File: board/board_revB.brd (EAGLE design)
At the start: 94 x 44.5 mm, 88 parts, among them IC1 MCP1703CB, Q1 ULN2003AS, Q2 ULN2003AD, Y1 8Mhz

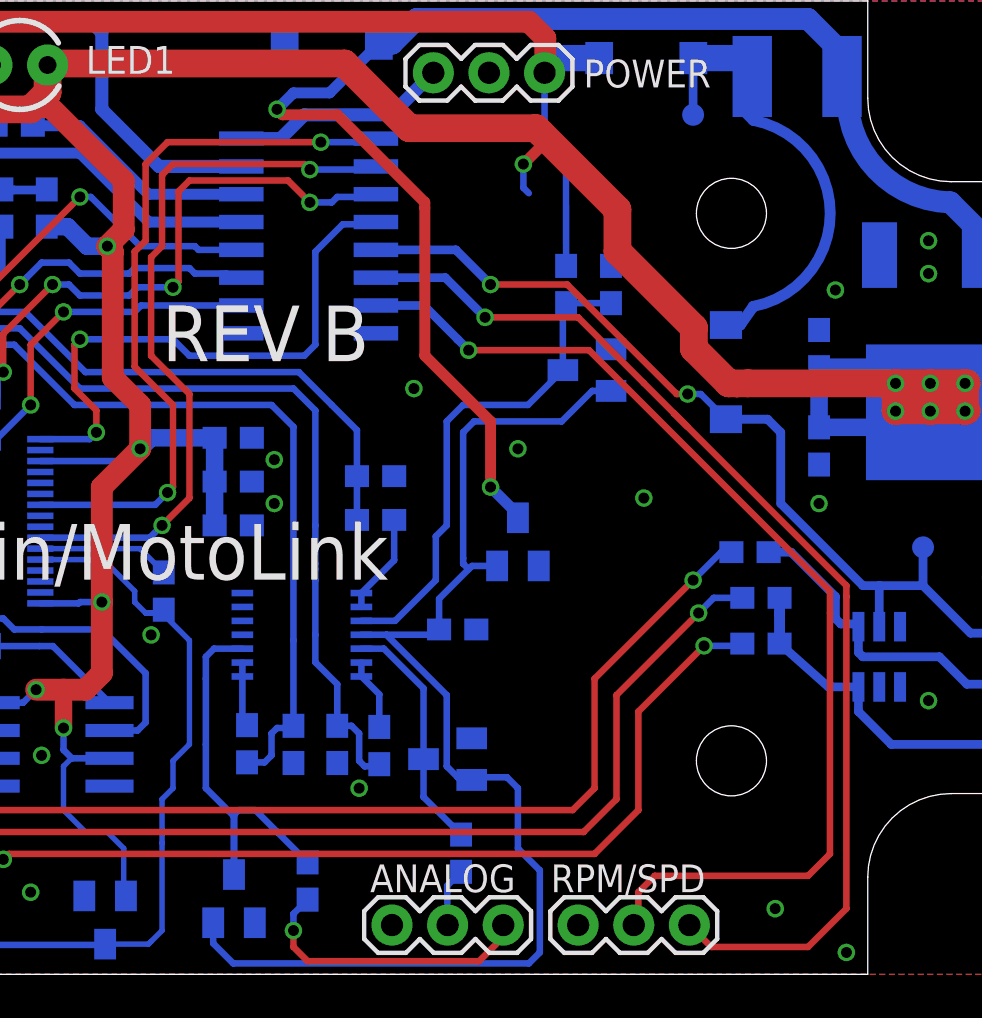
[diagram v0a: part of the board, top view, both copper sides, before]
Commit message: [Code] Now using CCM for ISRs and time critical threads
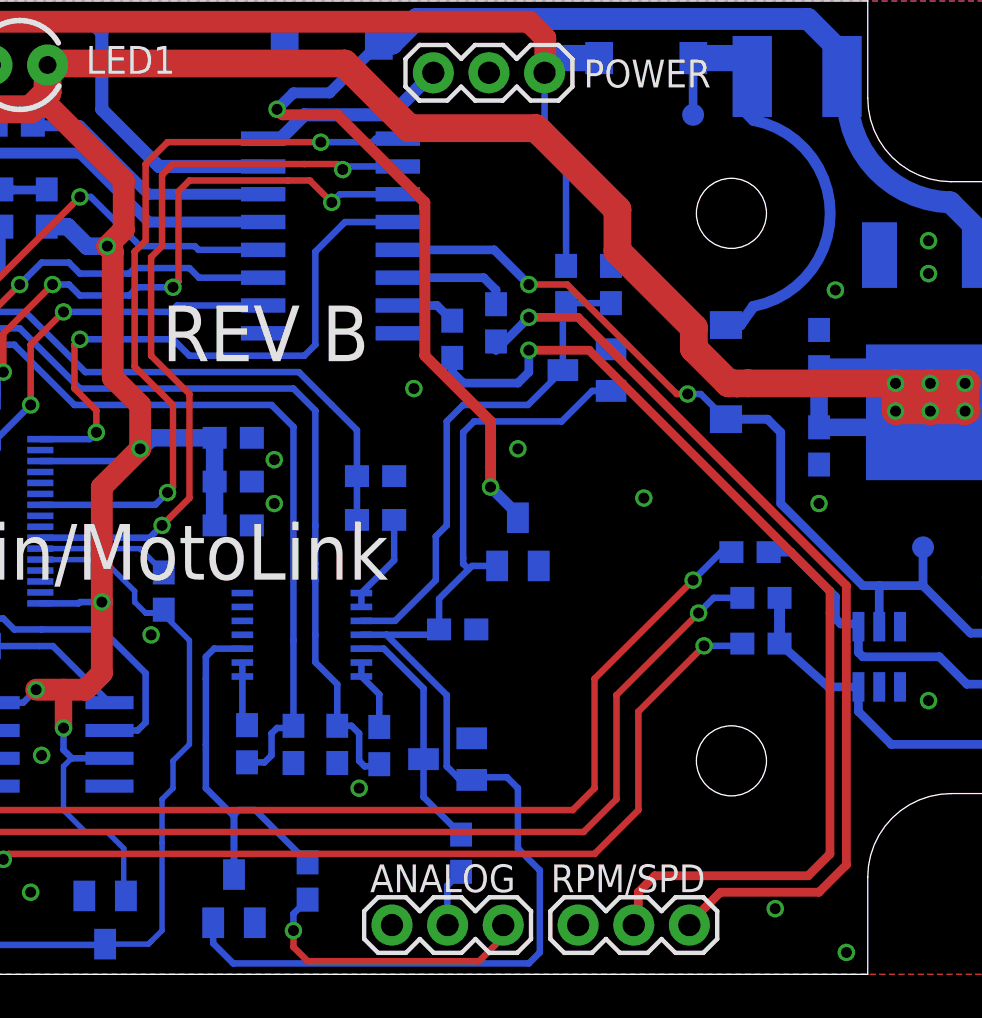
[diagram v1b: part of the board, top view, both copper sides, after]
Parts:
- added R25, R26: 1K, SparkFun-Resistors:0603-RES
- moved Q2 1.00 mm to (61.2, 33.7)
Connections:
- new net N$12: CON_RPM-VSS.3, R25.1
- new net N$9: Q2.7, R26.2
- net N$16: now also R25.2; no longer CON_RPM-VSS.3
- net N$21: now also R26.1; no longer Q2.7
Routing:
- net N$16: track 51.3 -> 5.37 mm, vias 1 -> 0
- net N$12: track 0.00 -> 43.2 mm, vias 0 -> 1
- net N$9: track 0.00 -> 2.77 mm
- net +3V3: track 305.6 -> 303.1 mm, vias 16 -> 15
- net N$21: track 49.2 -> 46.9 mm
- net FREQ1_IN: track 29.0 -> 30.0 mm
- net SCS_TRIG: track 33.3 -> 34.4 mm
- net LED1_TRIG: track 26.2 -> 27.3 mm
- net LED2_TRIG: track 26.3 -> 27.3 mm
- net USB_VBUS: track 41.6 -> 40.6 mm
- net USB_DETECT: track 24.1 -> 25.1 mm
- net SCS: track 69.7 -> 70.7 mm
- net RELAY_TRIG: track 33.1 -> 34.1 mm
- net RELAY_OUT: track 10.0 -> 9.01 mm
- net N$15: track 10.8 -> 11.8 mm
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
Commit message: [Board] Updates
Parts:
- added ESP: ESP8266, misc:ESP-03
- IC_FRAM: value 25LC080SN -> FM25L04B
- renumbered IC_EE to IC_FRAM
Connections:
- net GND: now also IC_OPA.12, IC_OPA.13
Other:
- board text added: "Github.com /fpoussin /MotoLink"
- board text removed: "Github.com/fpoussin/MotoLink"
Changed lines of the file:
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@@
 <wire x1="89.535" y1="36.195" x2="93.98" y2="36.195" width="0" layer="20"/>
 <wire x1="93.98" y1="36.195" x2="93.98" y2="8.255" width="0" layer="20"/>
-<text x="16.3125" y="21.33" size="3.81" layer="21" font="vector" ratio="16">MotoLink</text>
-<text x="16.2075" y="18.025" size="2.54" layer="21" font="vector" ratio="16" distance="0">Github.com/fpoussin/MotoLink</text>
+<text x="18.8125" y="21.33" size="3.81" layer="21" font="vector" ratio="16">MotoLink</text>
+<text x="73.2075" y="19.525" size="2.54" layer="21" font="vector" ratio="14" distance="30">Github.com
+/fpoussin
+/MotoLink</text>
 <wire x1="30.955" y1="14.94" x2="40.6625" y2="14.94" width="0.254" layer="21"/>
 <wire x1="40.6625" y1="14.94" x2="40.6625" y2="4.4625" width="0.254" layer="21"/>
@@
 <text x="23.3825" y="8.495" size="1.27" layer="21" font="vector" ratio="16" rot="R180">1</text>
 <text x="29.99" y="4.245" size="1.27" layer="21" font="vector" ratio="16" rot="R180">6</text>
-<text x="53.5" y="28" size="2.54" layer="21" font="vector" ratio="14" distance="40">REV B</text>
+<text x="25" y="18" size="2.54" layer="21" font="vector" ratio="14" distance="30">REV B</text>
 <text x="5.25" y="24.25" size="1.27" layer="25" font="vector" ratio="16" rot="R90">K-LINE</text>
 <text x="5.25" y="18" size="1.27" layer="25" font="vector" ratio="16" rot="R90">CAN</text>
@@
 <attribute name="VALUE" x="84.75" y="38.025" size="1.016" layer="28" rot="MR0"/>
 </element>
-<element name="IC_EE" library="microchip" package="SO-08" value="25LC080SN" x="48.5" y="10.5" smashed="yes" rot="MR270">
+<element name="IC_FRAM" library="microchip" package="SO-08" value="FM25L04B" x="48.5" y="10.5" smashed="yes" rot="MR270">
 <attribute name="OC_NEWARK" value="96K4092" x="48.5" y="10.5" size="1.778" layer="28" rot="MR270" display="off"/>
 <attribute name="MPN" value="25LC080/SN" x="48.5" y="10.5" size="1.778" layer="28" rot="MR270" display="off"/>
 <attribute name="MF" value="MICROCHIP" x="48.5" y="10.5" size="1.778" layer="28" rot="MR270" display="off"/>
 <attribute name="OC_FARNELL" value="1137302" x="48.5" y="10.5" size="1.778" layer="28" rot="MR270" display="off"/>
-<attribute name="NAME" x="51.405" y="13.417" size="1.27" layer="26" font="vector" ratio="16" rot="MR0"/>
+<attribute name="NAME" x="52.655" y="13.417" size="1.27" layer="26" font="vector" ratio="16" rot="MR0"/>
 <attribute name="VALUE" x="50.405" y="6.563" size="1.27" layer="28" rot="MR0"/>
 </element>
@@
 <attribute name="VALUE" x="65.607" y="27.984" size="0.4064" layer="28" font="vector" rot="MR90"/>
 </element>
+<element name="ESP" library="misc" package="ESP-03" value="ESP8266" x="64.5" y="17.75"/>
 </elements>
 <signals>
@@
 <contactref element="C6" pad="2"/>
 <contactref element="C8" pad="1"/>
-<via x="53" y="15.5" extent="1-16" drill="0.5"/>
+<via x="53" y="15.25" extent="1-16" drill="0.5"/>
 <via x="39.75" y="20.75" extent="1-16" drill="0.5"/>
 <via x="11.5" y="39.5" extent="1-16" drill="0.5"/>
@@
 <via x="38.25" y="9.25" extent="1-16" drill="0.5"/>
 <via x="48" y="10" extent="1-16" drill="0.5"/>
-<via x="62.5" y="8.5" extent="1-16" drill="0.5"/>
-<via x="81.5" y="3" extent="1-16" drill="0.5"/>
+<via x="60.5" y="12.75" extent="1-16" drill="0.5"/>
 <via x="88.5" y="32" extent="1-16" drill="0.5"/>
 <via x="32" y="34.25" extent="1-16" drill="0.5"/>
@@
 <via x="1" y="16.5" extent="1-16" drill="0.5"/>
 <via x="4.25" y="33.25" extent="1-16" drill="0.5"/>
-<contactref element="IC_EE" pad="4"/>
+<contactref element="IC_FRAM" pad="4"/>
 <contactref element="R20" pad="2"/>
 <contactref element="R19" pad="2"/>
@@
 <contactref element="IC1" pad="1"/>
 <via x="84.75" y="1" extent="1-16" drill="0.5"/>
+<via x="68.25" y="36" extent="1-16" drill="0.5"/>
+<contactref element="IC_OPA" pad="12"/>
+<contactref element="IC_OPA" pad="13"/>
 </signal>
 <signal name="+3V3">
@@
 <wire x1="41.725" y1="41.525" x2="41.7" y2="41.5" width="1.27" layer="1"/>
 <wire x1="70.8025" y1="38.4175" x2="70.8025" y2="37.8025" width="0.3" layer="1"/>
-<wire x1="47.94" y1="16.94" x2="49.69" y2="16.94" width="0.3" layer="16"/>
-<wire x1="49.69" y1="16.94" x2="49.75" y2="17" width="0.3" layer="16"/>
-<wire x1="49.75" y1="17" x2="50.75" y2="17" width="0.3" layer="16"/>
+<wire x1="47.94" y1="16.94" x2="50.69" y2="16.94" width="0.3" layer="16"/>
+<wire x1="50.69" y1="16.94" x2="50.75" y2="17" width="0.3" layer="16"/>
 <via x="50.75" y="17" extent="1-16" drill="0.5"/>
 <wire x1="50.75" y1="17" x2="50.75" y2="22.25" width="1" layer="1"/>
@@
 <wire x1="51.25" y1="33" x2="51" y2="33.25" width="1" layer="1"/>
 <contactref element="STM32" pad="13"/>
-<contactref element="STM32" pad="1"/>
-<wire x1="38.49" y1="26.39" x2="38.49" y2="25.68" width="0.3" layer="16"/>
-<wire x1="38.49" y1="25.68" x2="37.905" y2="25.095" width="0.3" layer="16"/>
-<wire x1="37.905" y1="25.095" x2="37.25" y2="24.44" width="0.3" layer="16"/>
 <wire x1="44.49" y1="26.39" x2="44.49" y2="24.99" width="0.3" layer="16"/>
 <wire x1="41.87" y1="24.75" x2="41.75" y2="24.75" width="0.3" layer="16"/>
 <wire x1="41.75" y1="24.75" x2="40.75" y2="23.75" width="0.3" layer="16"/>
-<wire x1="40.75" y1="23.75" x2="39.25" y2="23.75" width="0.3" layer="16"/>
-<wire x1="39.25" y1="23.75" x2="37.905" y2="25.095" width="0.3" layer="16"/>
+<wire x1="40.75" y1="23.75" x2="38.5" y2="23.75" width="0.3" layer="16"/>
 <wire x1="39.5" y1="0.5" x2="24.25" y2="0.5" width="0.4" layer="1"/>
 <wire x1="22.5" y1="6.0725" x2="24.3425" y2="7.915" width="0.4" layer="1"/>
@@
 <wire x1="92.5" y1="26" x2="90.4525" y2="26" width="0.4" layer="16"/>
 <wire x1="90.4525" y1="26" x2="90.17" y2="25.7175" width="0.4" layer="16"/>
-<wire x1="50.9" y1="16.85" x2="50.75" y2="17" width="0.3" layer="16"/>
 <via x="47.75" y="13" extent="1-16" drill="0.5"/>
 <wire x1="50.75" y1="17" x2="50.75" y2="13.75" width="1" layer="1"/>
@@
 <via x="49" y="11.25" extent="1-16" drill="0.5"/>
 <wire x1="49" y1="11.25" x2="49" y2="13" width="0.8" layer="1"/>
-<contactref element="IC_EE" pad="7"/>
-<contactref element="IC_EE" pad="8"/>
-<contactref element="IC_EE" pad="3"/>
+<contactref element="IC_FRAM" pad="7"/>
+<contactref element="IC_FRAM" pad="8"/>
+<contactref element="IC_FRAM" pad="3"/>
 <wire x1="45.9" y1="11.135" x2="45.9" y2="12.405" width="0.3" layer="16"/>
 <wire x1="51.1" y1="9.865" x2="49.385" y2="9.865" width="0.3" layer="16"/>
@@
 <wire x1="51.75" y1="5.75" x2="51.75" y2="3.68" width="0.25" layer="16"/>
 <wire x1="51.75" y1="3.68" x2="51.85" y2="3.58" width="0.25" layer="16"/>
+<wire x1="37.25" y1="24.44" x2="37.81" y2="24.44" width="0.3" layer="16"/>
+<wire x1="37.81" y1="24.44" x2="38.5" y2="23.75" width="0.3" layer="16"/>
+<contactref element="STM32" pad="1"/>
+<wire x1="38.49" y1="26.39" x2="38.49" y2="25.12" width="0.3" layer="16"/>
+<wire x1="38.49" y1="25.12" x2="37.81" y2="24.44" width="0.3" layer="16"/>
 </signal>
 <signal name="+12V">
@@
 <wire x1="44.49" y1="13.99" x2="43.5" y2="13" width="0.3" layer="16"/>
 <wire x1="43.5" y1="13" x2="43.5" y2="10.5" width="0.3" layer="16"/>
-<contactref element="IC_EE" pad="5"/>
+<contactref element="IC_FRAM" pad="5"/>
 <wire x1="45.9" y1="8.595" x2="44.405" y2="8.595" width="0.3" layer="16"/>
 <wire x1="44.405" y1="8.595" x2="43.5" y2="9.5" width="0.3" layer="16"/>
@@
 <wire x1="46.25" y1="16.25" x2="46.75" y2="15.75" width="0.3" layer="16"/>
 <wire x1="46.75" y1="15.75" x2="48" y2="15.75" width="0.3" layer="16"/>
-<contactref element="IC_EE" pad="2"/>
+<contactref element="IC_FRAM" pad="2"/>
 <wire x1="48" y1="15.75" x2="50.75" y2="15.75" width="0.3" layer="16"/>
 <wire x1="50.75" y1="15.75" x2="52.75" y2="13.75" width="0.3" layer="16"/>
@@
 <signal name="SPI2_SCK">
 <contactref element="STM32" pad="34"/>
-<contactref element="IC_EE" pad="6"/>
+<contactref element="IC_FRAM" pad="6"/>
 <wire x1="45.9" y1="9.865" x2="44.635" y2="9.865" width="0.3" layer="16"/>
 <wire x1="44.635" y1="9.865" x2="44" y2="10.5" width="0.3" layer="16"/>
@@
 <contactref element="STM32" pad="33"/>
 <wire x1="45.99" y1="14.99" x2="47.91" y2="14.99" width="0.3" layer="16"/>
-<contactref element="IC_EE" pad="1"/>
+<contactref element="IC_FRAM" pad="1"/>
 <wire x1="47.91" y1="14.99" x2="48.515" y2="14.99" width="0.3" layer="16"/>
 <wire x1="48.515" y1="14.99" x2="51.1" y2="12.405" width="0.3" layer="16"/>
@@
 <wire x1="52.75" y1="16.5" x2="53.5" y2="16.5" width="0.25" layer="16"/>
 <wire x1="53.5" y1="16.5" x2="54.75" y2="15.25" width="0.25" layer="16"/>
-<wire x1="54.75" y1="15.25" x2="54.75" y2="10.5" width="0.25" layer="16"/>
-<wire x1="54.75" y1="10.5" x2="54" y2="9.75" width="0.25" layer="16"/>
-<wire x1="54" y1="9.75" x2="54" y2="8.5" width="0.25" layer="16"/>
-<wire x1="54" y1="8.5" x2="53.5" y2="8" width="0.25" layer="16"/>
-<wire x1="53.5" y1="8" x2="53.5" y2="6" width="0.25" layer="16"/>
+<wire x1="54.75" y1="15.25" x2="54.75" y2="9" width="0.25" layer="16"/>
+<wire x1="54.75" y1="9" x2="54" y2="8.25" width="0.25" layer="16"/>
+<wire x1="54" y1="8.25" x2="53.5" y2="7.75" width="0.25" layer="16"/>
+<wire x1="53.5" y1="7.75" x2="53.5" y2="6" width="0.25" layer="16"/>
 <wire x1="44.77" y1="1.345" x2="50.865" y2="1.345" width="0.3" layer="16"/>
 <wire x1="50.865" y1="1.345" x2="50.9" y2="1.38" width="0.3" layer="16"/>
@@
 </board>
 </drawing>
+<compatibility>
+<note version="6.3" minversion="6.2.2" severity="warning">
+Since Version 6.2.2 text objects can contain more than one line,
+which will not be processed correctly with this version.
+</note>
+</compatibility>
 </eagle>

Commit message: [code] updated ChibiOS
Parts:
- removed ESP: ESP8266, misc:ESP-03
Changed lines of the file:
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@@
 <?xml version="1.0" encoding="utf-8"?>
 <!DOCTYPE eagle SYSTEM "eagle.dtd">
-<eagle version="7.1.0">
+<eagle version="7.3.0">
 <drawing>
 <settings>
@@
 <attribute name="VALUE" x="65.607" y="27.984" size="0.4064" layer="28" font="vector" rot="MR90"/>
 </element>
-<element name="ESP" library="misc" package="ESP-03" value="ESP8266" x="64.5" y="17.75"/>
 </elements>
 <signals>

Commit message: [Board] Working on Rev B
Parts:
- removed C22, C9: 100nF, SparkFun-Capacitors:0603-CAP
- removed Q1: ULN2003AS, misc:SSOP16
- removed R18, R9: 4.7K, SparkFun-Resistors:0603-RES
- added C10, C11, C12, C13: 100nF, SparkFun-Capacitors:0603-CAP
- added U1: MAX202, SparkFun-DigitalIC:TSSOP16
- CON_AN, CON_KNK, CON_PWR, CON_RPM-VSS: device SparkFun-Connectors:1X03 -> SparkFun-Connectors:1X03_LOCK
- CON_CAN, CON_K-LINE, CON_UART1, CON_UART2: value M02PTH -> M02LOCK; device SparkFun-Connectors:1X02 -> SparkFun-Connectors:1X02_LOCK
- D6: device SparkFun-DiscreteSemi:SMA-DIODE -> SparkFun-DiscreteSemi:SOD-323
- moved CON_UART2 2.50 mm to (12.0, 2.25), turned to 0 degrees
- moved D6 1.95 mm to (4.50, 24.2), turned to 270 degrees
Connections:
- new net N$20: C11.2, U1.4
- new net N$22: C11.1, U1.5
- new net N$23: C10.1, U1.3
- new net N$26: C10.2, U1.1
- new net N$27: C12.2, U1.6
- new net N$29: C13.2, U1.2
- net +12V: now also D6.2; no longer D6.A, R18.2, R9.2
- net +3V3: now also C13.1, U1.16
- net BUT1: no longer C22.1
- net BUT2: no longer C9.1
- net GND: now also C12.1, U1.15; no longer C22.2, C9.2, Q1.8
- net N$13: now also D6.1; no longer D6.C
- net UART2_RXD_OUT: now also U1.13; no longer Q1.3
- net UART2_TXD_OUT: now also U1.14; no longer Q1.12, R9.1
- net UART3_RXD_OUT: now also U1.8; no longer Q1.1
- net UART3_TXD_OUT: now also U1.7; no longer Q1.10, R18.1
- net USART2_RX: now also U1.12; no longer Q1.14
- net USART2_TX: now also U1.11; no longer Q1.5
- net USART3_RX: now also U1.9; no longer Q1.16
- net USART3_TX: now also U1.10; no longer Q1.7
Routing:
- net +12V: track 144.7 -> 106.5 mm, vias 4 -> 2
- net UART2_TXD_OUT: track 20.2 -> 0.00 mm
- net UART3_TXD_OUT: track 16.1 -> 0.00 mm
- net UART2_RXD_OUT: track 14.7 -> 0.00 mm
- net USART3_RX: track 35.4 -> 27.0 mm, vias 2 -> 1
- net USART2_RX: track 33.8 -> 27.5 mm
- net USART2_TX: track 36.2 -> 30.8 mm, vias 2 -> 1
- net USART3_TX: track 35.9 -> 31.0 mm, vias 2 -> 1
- net UART3_RXD_OUT: track 2.67 -> 0.00 mm
- net N$13: track 3.11 -> 4.63 mm
